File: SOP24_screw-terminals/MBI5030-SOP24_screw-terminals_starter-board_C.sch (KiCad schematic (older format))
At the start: 34 parts, among them P1 CONN_12, P2 CONN_12

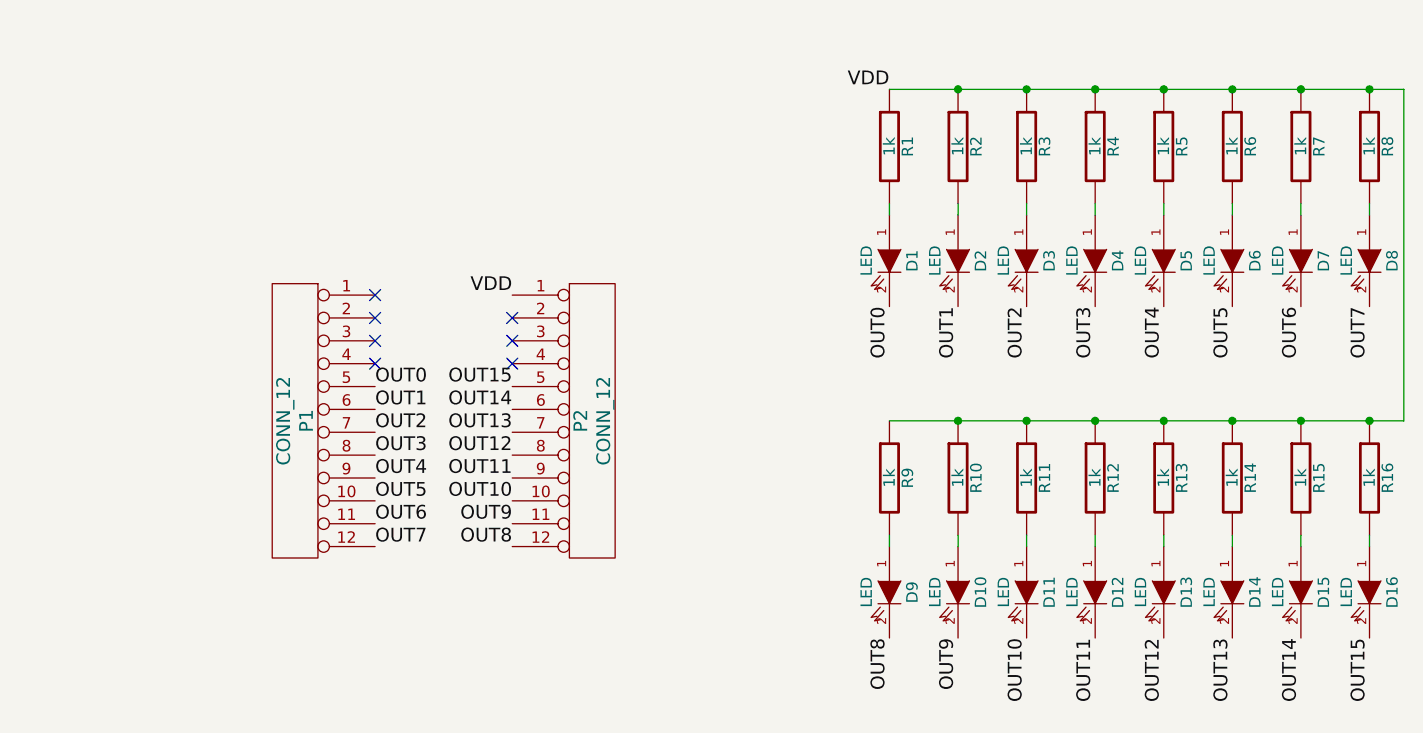
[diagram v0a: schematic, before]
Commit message: Playing with the screw-terminal variant. Terminal blocks are HUGE ;-(
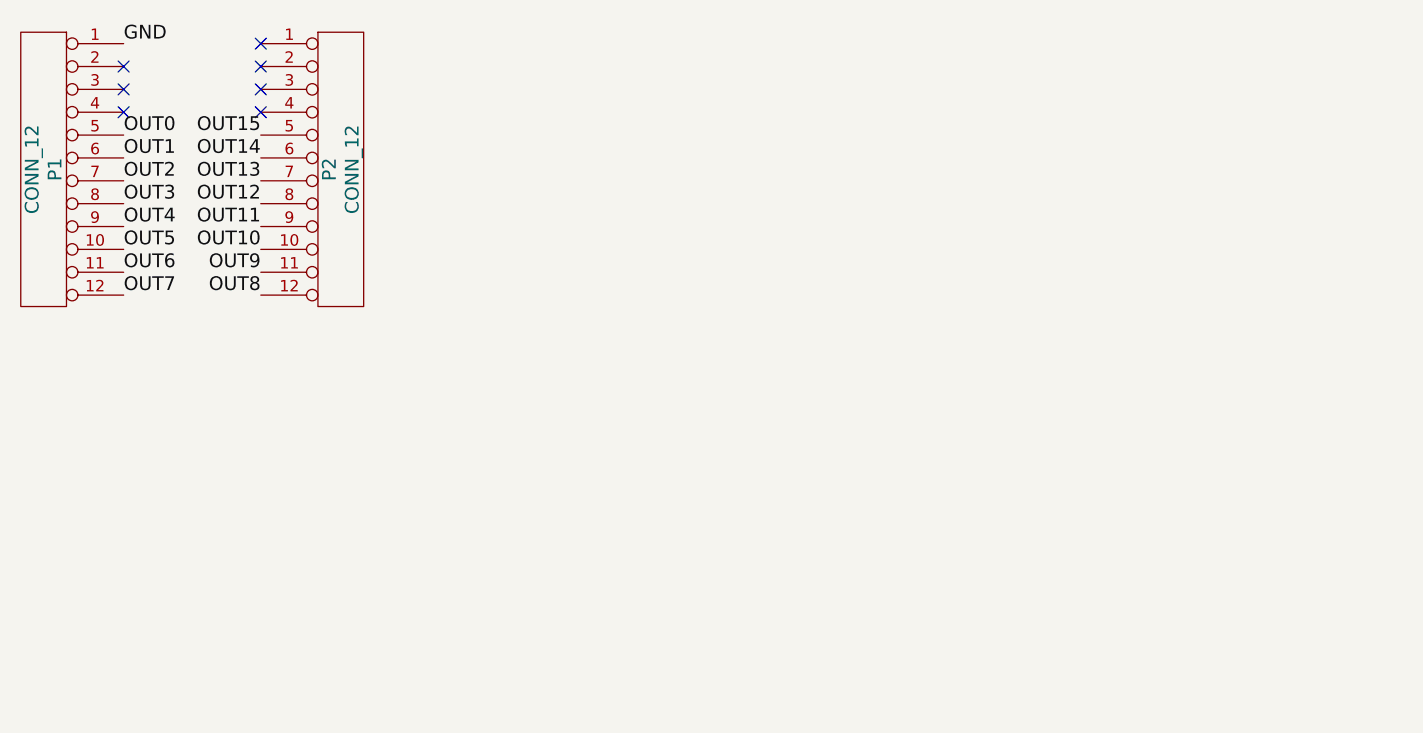
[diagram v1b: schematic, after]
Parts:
- removed D1, D10, D11, D12, D13, D14, D15, D16, D2, D3, D4, D5, D6, D7, D8, D9: LED, symbol LED
- removed R1, R10, R11, R12, R13, R14, R15, R16, R2, R3, R4, R5, R6, R7, R8, R9: 1k, symbol R
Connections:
- net GND: now reaches P1.1 (P1)
- net VDD: no longer names the net of P2.1 (P1)
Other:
- moved on the sheet: P1, P2
